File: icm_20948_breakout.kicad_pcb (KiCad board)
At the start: 2 copper layers, 22.8 x 18 mm, 16 parts, among them J1 Conn_01x07, U1 SN74LVC2T45YZP, U2 SN74LVC2T45YZP, U3 SN74LVC1T45DRL, U4 TLV70018DCKR, U5 ICM-20948

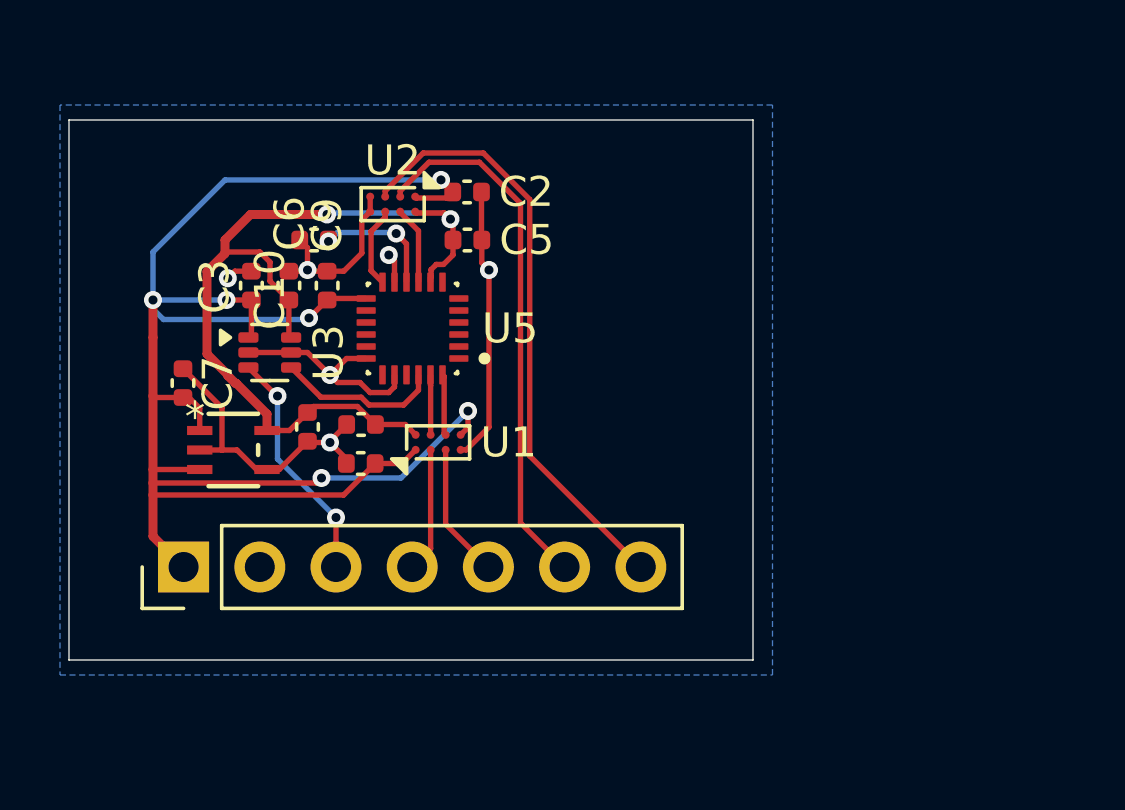
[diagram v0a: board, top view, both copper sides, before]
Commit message: Revised footprints and re-designed PCB
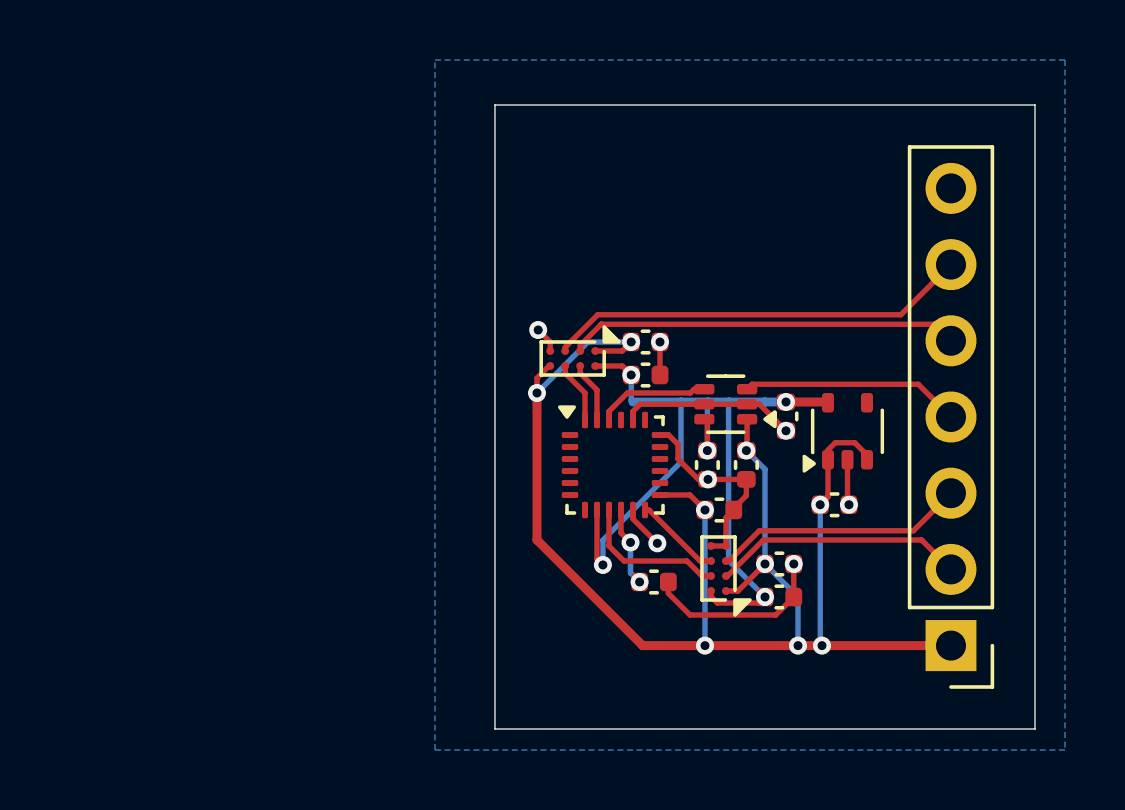
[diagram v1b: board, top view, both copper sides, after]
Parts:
- U4: value TLV70018DCKR -> ICM-20948; footprint Texas-Instruments-TLV70018DCKR:DCK5 -> Sensor_Motion:InvenSense_QFN-24_3x3mm_P0.4mm
- U5: value ICM-20948 -> TLV70018_SOT353; footprint ICM_20948:QFN40P300X300X105-24N -> Package_TO_SOT_SMD:SOT-353_SC-70-5
- moved J1 25.7 mm to (136.2, 93.5), turned to 180 degrees
- moved C7 22.1 mm to (132.3, 88.8), turned to 180 degrees
- moved C3 17.5 mm to (129.4, 87.5), turned to 90 degrees
- moved U2 16.3 mm to (128.4, 91.0), turned to 180 degrees
- moved C2 16.2 mm to (130.5, 90.8)
- moved C10 16.1 mm to (126.3, 91.4), turned to 0 degrees
- moved C8 16.0 mm to (130.7, 85.9)
- moved C5 15.8 mm to (130.5, 91.9)
- moved U3 15.3 mm to (128.7, 85.5), turned to 180 degrees
- moved C6 15.2 mm to (128.1, 87.5), turned to 90 degrees
- moved C9 15.1 mm to (128.5, 89.0), turned to 0 degrees
- moved U5 14.9 mm to (132.8, 86.4), turned to 90 degrees
- moved U4 12.7 mm to (125.0, 87.5)
- moved C1 10.3 mm to (126.0, 83.4), turned to 180 degrees
- moved C4 9.63 mm to (126.0, 84.5), turned to 180 degrees
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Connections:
- C10 pad 1: Net-(U5-REGOUT) -> Net-(U4-REGOUT)
- J1 pad 2: GND -> /SPI_MISO
- J1 pad 3: /ICM_CS_3V3 -> /ICM_INT_3V3
- J1 pad 4: /SPI_SCK -> /ICM_CS_3V3
- J1 pad 5: /SPI_MOSI -> /SPI_SCK
- J1 pad 6: /SPI_MISO -> /SPI_MOSI
- J1 pad 7: /ICM_INT_3V3 -> GND
- U4 pad 1: +3.3V -> unconnected-(U4-NC-Pad1)
- U4 pad 2: GND -> unconnected-(U4-NC-Pad2)
- U4 pad 3: +3.3V -> unconnected-(U4-NC-Pad3)
- U4 pad 4: GND -> unconnected-(U4-NC-Pad4)
- U4 pad 5: +1V8 -> unconnected-(U4-NC-Pad5)
- U5 pad 1: unconnected-(U5-NC-Pad1) -> +3.3V
- U5 pad 2: unconnected-(U5-NC__1-Pad2) -> GND
- U5 pad 3: unconnected-(U5-NC__2-Pad3) -> +3.3V
- U5 pad 5: unconnected-(U5-NC__4-Pad5) -> +1V8
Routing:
- net /ICM_INT_3V3: track 20.0 -> 8.44 mm
- net +3.3V: track 61.6 -> 51.2 mm, vias 6 -> 9
- net GND: track 34.3 -> 23.8 mm, vias 6 -> 7
- net /SPI_MOSI: track 4.50 -> 14.1 mm
- net /SPI_MISO: track 17.9 -> 8.40 mm
- net /SPI_SCK: track 4.16 -> 13.1 mm
- net Net-(U5-REGOUT): track 4.16 -> 0.00 mm, vias 2 -> 0
- net Net-(U4-REGOUT): track 0.00 -> 2.66 mm, vias 0 -> 2
- net /ICM_MISO: track 2.60 -> 5.01 mm
- net /ICM_CS_1V8: track 5.48 -> 3.77 mm
- net /ICM_CS_3V3: track 7.87 -> 7.32 mm, vias 2 -> 0
- net +1V8: track 29.5 -> 29.1 mm, vias 2 -> 5
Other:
- board size 22.8 x 18 mm -> 18 x 20.8 mm

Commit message: generated gerbers for v1
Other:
- board text added: "ICM-20948 + level shifters"
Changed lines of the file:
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@@
 			(plot_on_all_layers_selection 0x00000000_00000000_00000000_00000000)
 			(disableapertmacros no)
-			(usegerberextensions no)
-			(usegerberattributes yes)
-			(usegerberadvancedattributes yes)
-			(creategerberjobfile yes)
+			(usegerberextensions yes)
+			(usegerberattributes no)
+			(usegerberadvancedattributes no)
+			(creategerberjobfile no)
 			(dashed_line_dash_ratio 12.000000)
 			(dashed_line_gap_ratio 3.000000)
@@
 			(outputformat 1)
 			(mirror no)
-			(drillshape 1)
+			(drillshape 0)
 			(scaleselection 1)
-			(outputdirectory "")
+			(outputdirectory "gerbers/")
 		)
 	)
@@
 		(layer "Edge.Cuts")
 	)
+	(gr_text "ICM-20948\n+ level shifters"
+		(at 122 80.3 0)
+		(layer "F.SilkS")
+		(effects
+			(font
+				(size 1 1)
+				(thickness 0.1)
+			)
+			(justify left bottom)
+		)
+	)
 	(segment
